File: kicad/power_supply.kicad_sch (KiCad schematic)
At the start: 16 parts, among them T1 reuse / AnTek AS-0524, U1 LM317T

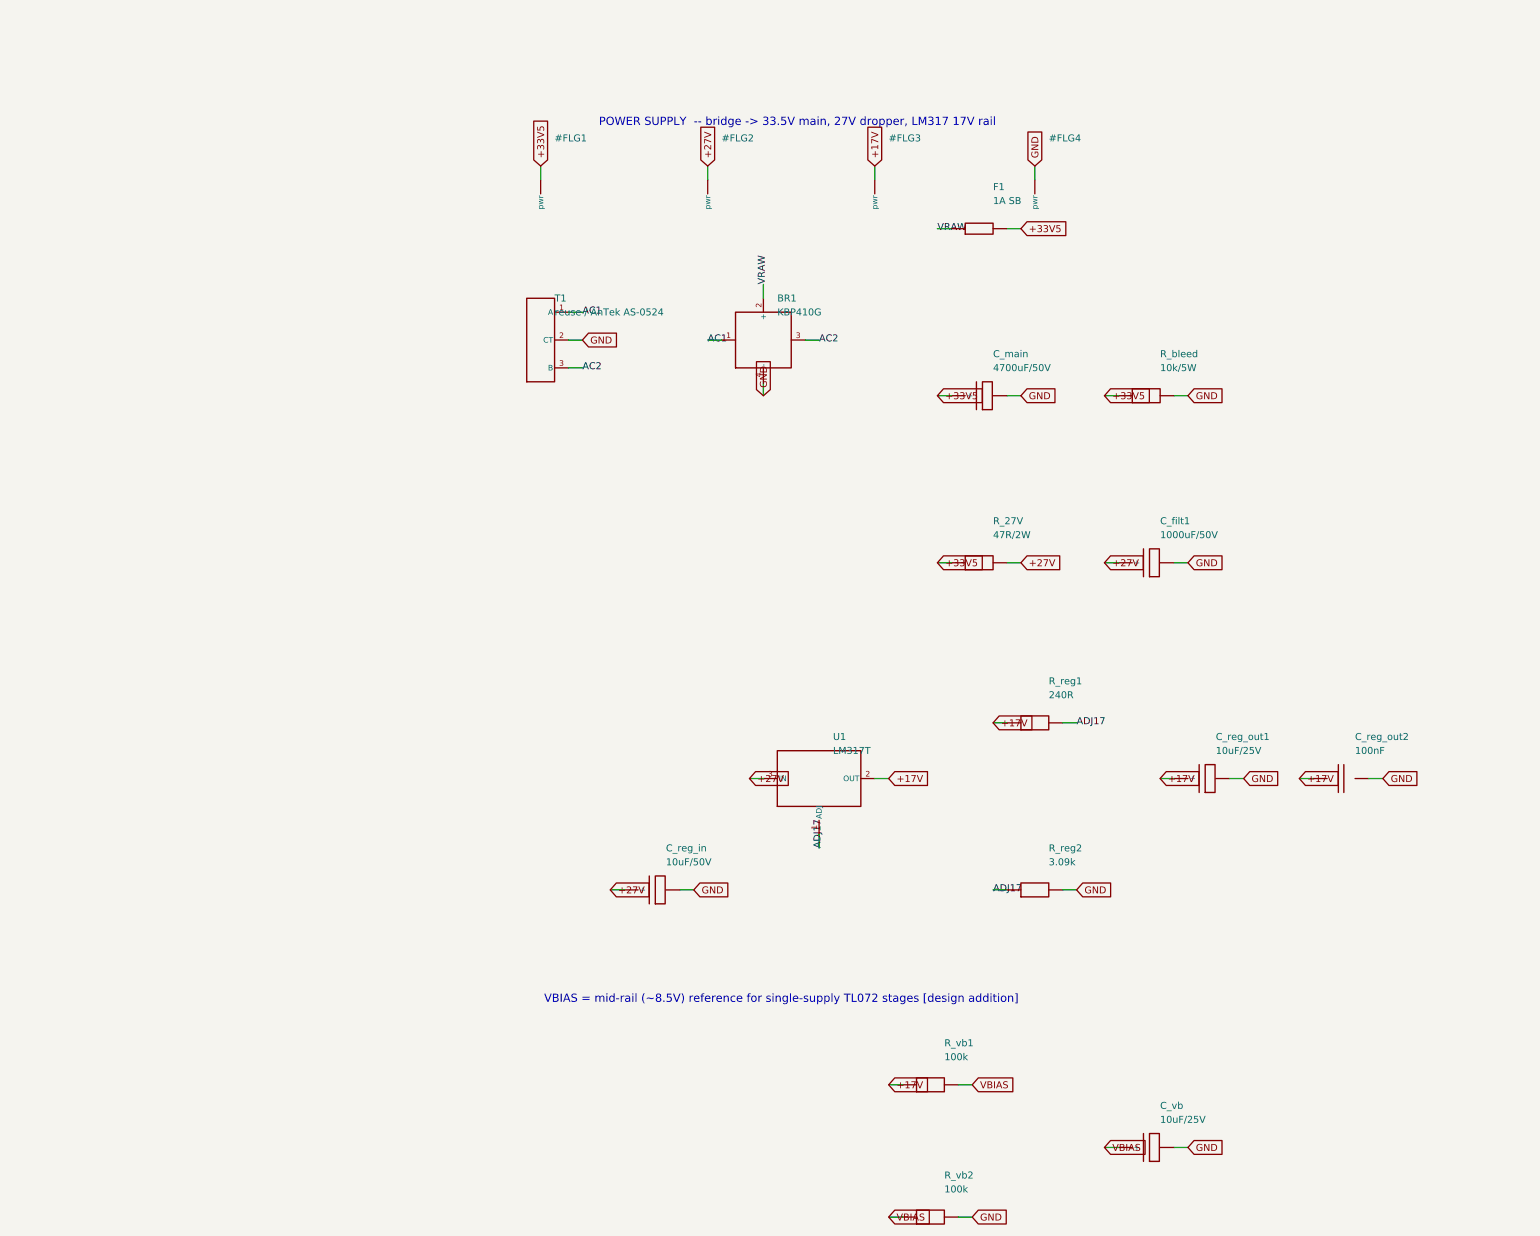
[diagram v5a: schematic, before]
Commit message: Keep LM317-input pre-filter (rename +27V->VREG_IN, 47R->100R) - corrected call
On reflection my earlier "delete R_27V, feed LM317 from +33.5V" recommendation
was wrong for a noise-conscious design: R_27V + C_filt1 is an RC pre-filter on
the LM317 input AND decouples the preamp supply from the power amp's transient
current draw on the +33.5V rail (the LM317's PSRR alone falls off with
frequency). Deleting it would hurt noise.

The real bug was the mislabeling: under the modern ~15 mA load the node sits at
~32 V, not 27 V, so the "27 V rail / 26-28 V" naming was a leftover misnomer.

Done instead:
- keep the element; bump 47R/2W -> 100R/1W (~6 dB more 120 Hz ripple rejection,
  ~1.5 V drop at 15 mA, LM317 in-out diff 14.7 V << 40 V max, ~0.02 W)
- rename net +27V -> VREG_IN (schematic gen, .kicad_pro Power pattern)
- correct the docs/troubleshooting voltages (~31-33 V) across Part 1/2/3/4,
  errata, BOM, availability-audit, PCB-NOTES/AUDIT, SCHEMATIC-BUILD, CHECKLIST

Verified: sch erc 0, full DRC unchanged (164), demo DRC 0, SPICE exit 0, BOM
CSV clean, net classes intact (VREG_IN now in the Power pattern).

https://claude.ai/code/session_01PkrfUi9tvZfLvudJ7h23qD
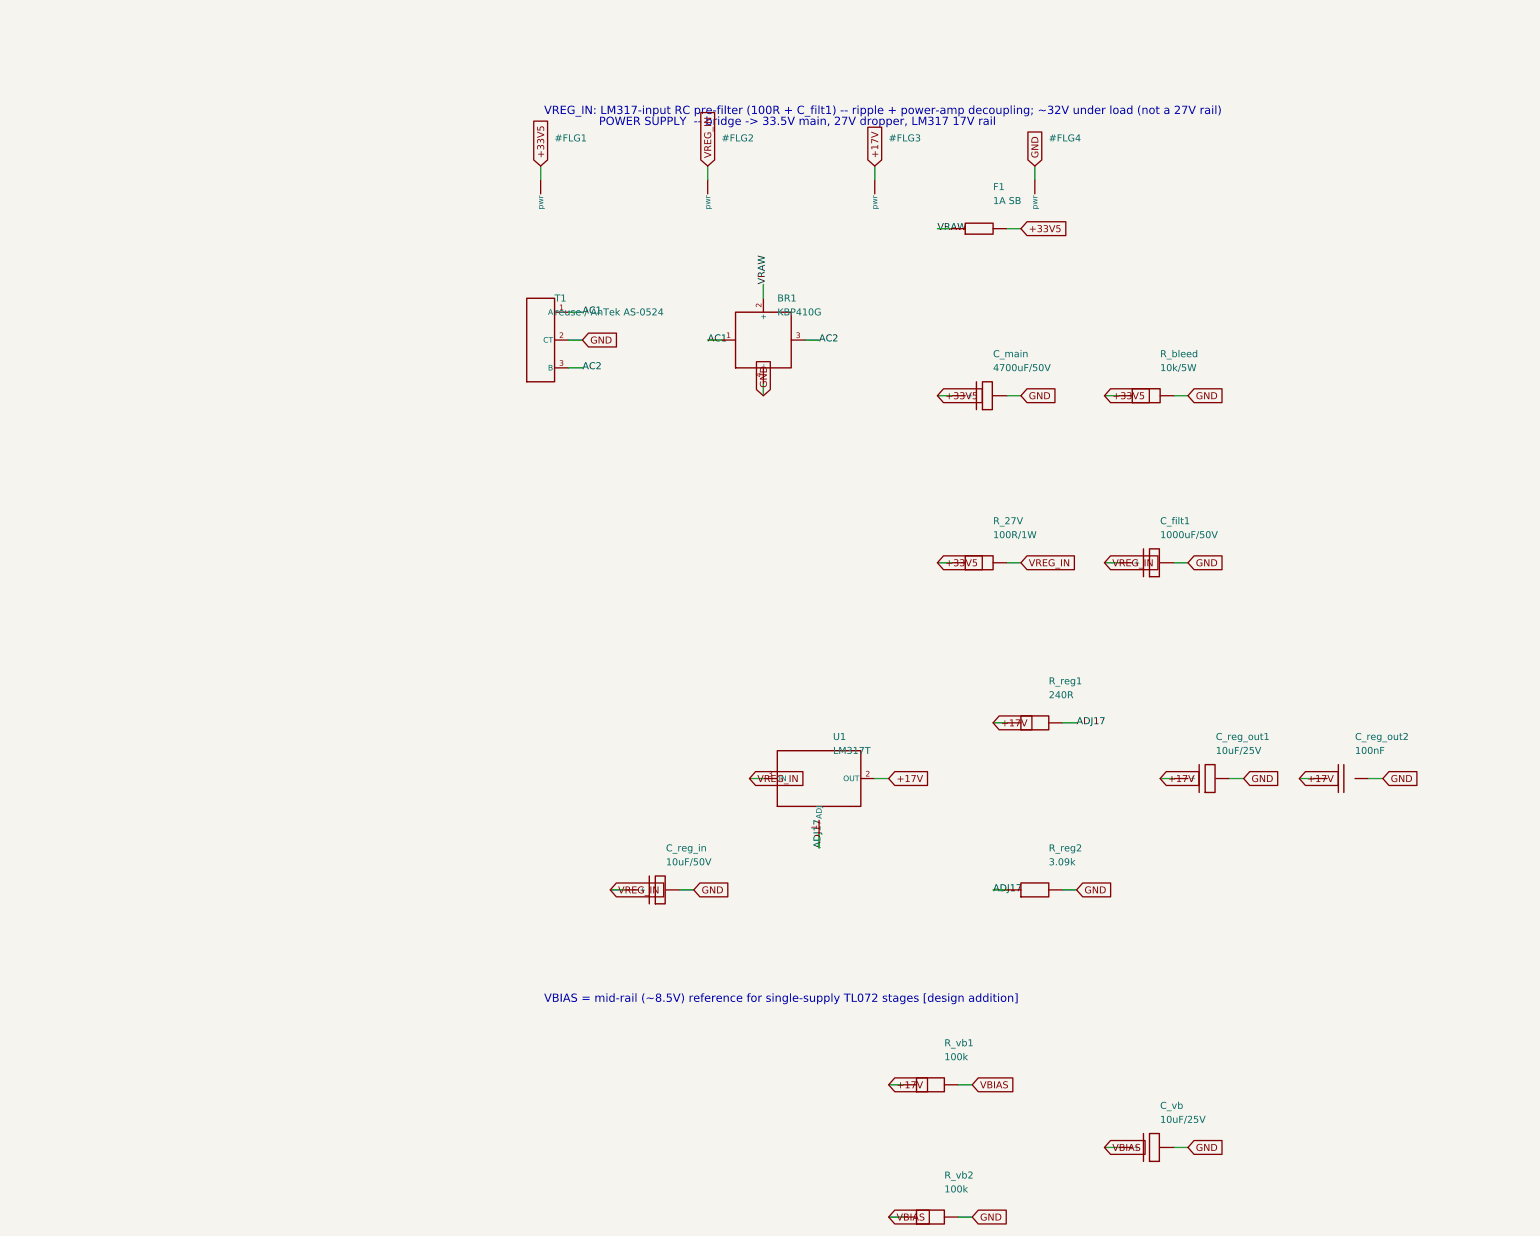
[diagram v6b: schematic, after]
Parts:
- R_27V: value 47R/2W -> 100R/1W
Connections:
- net +27V renamed VREG_IN
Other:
- note added: "VREG_IN: LM317-input RC pre-filter (100R + C_filt1) -- ripple + power-amp decoupling; ~32V under load (not a 27V rail)"

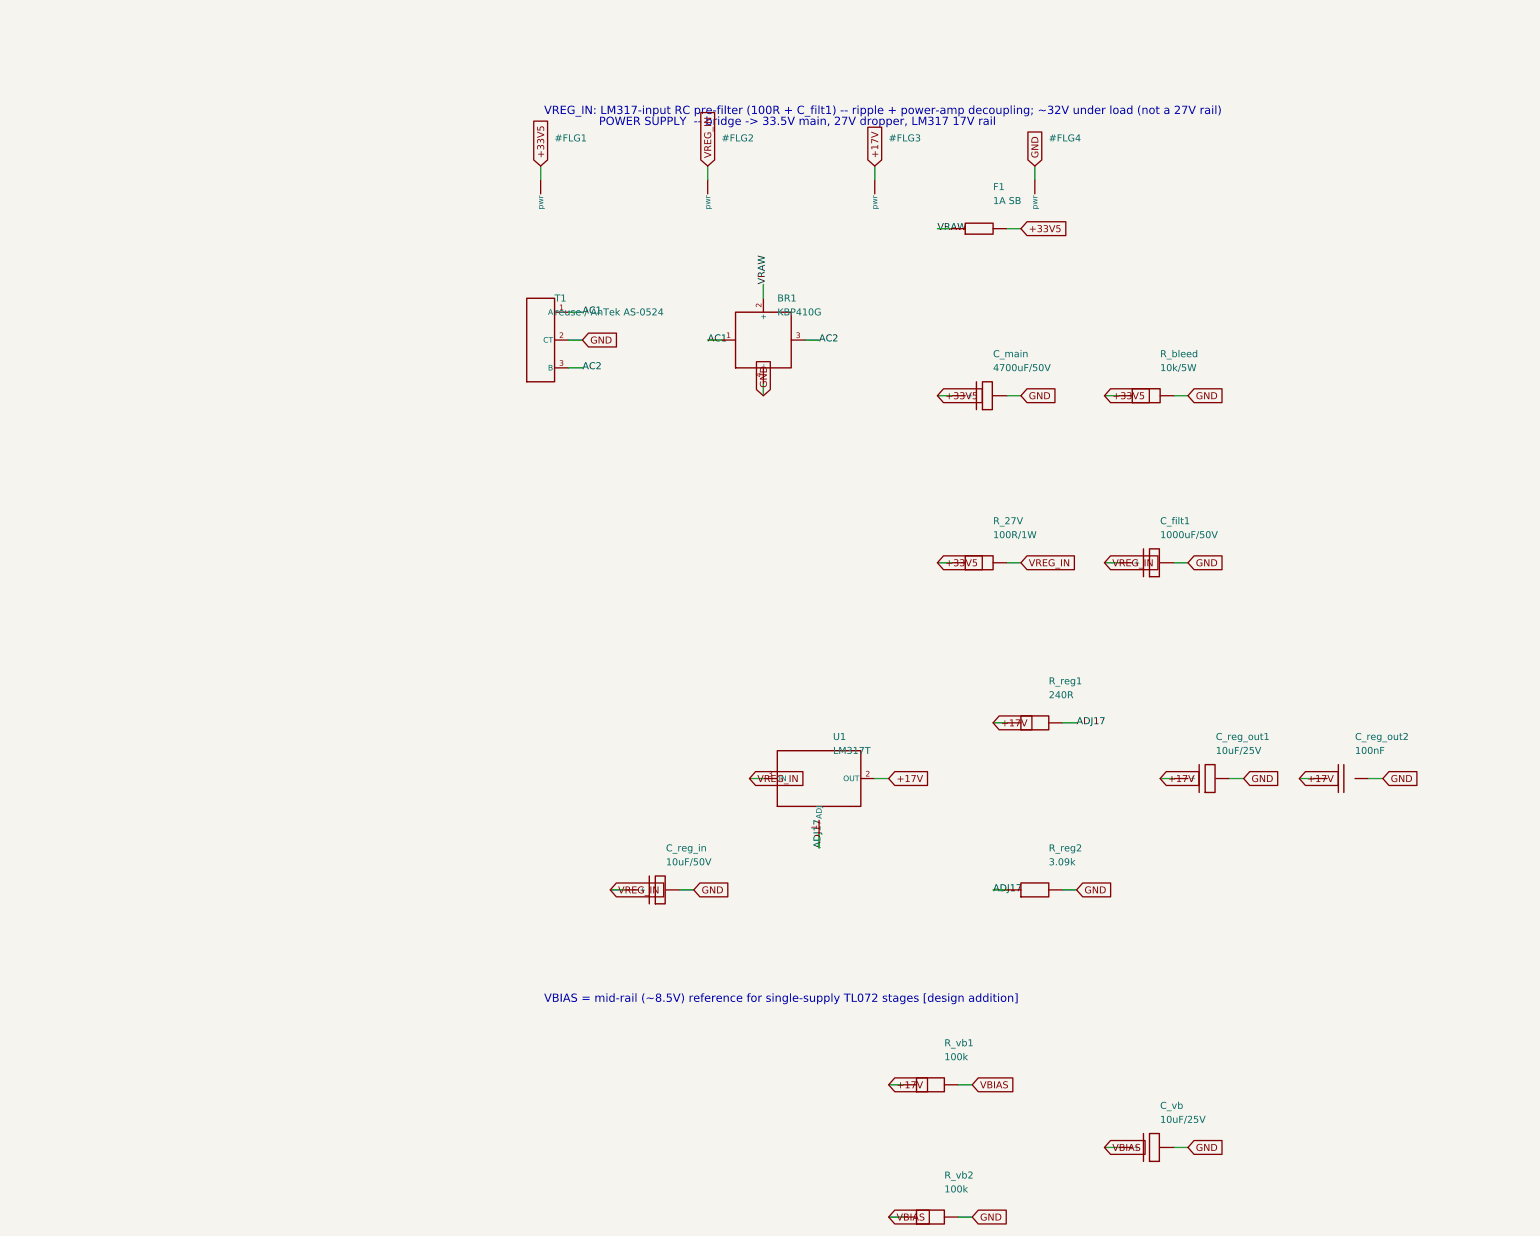
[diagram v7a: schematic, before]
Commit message: Redesign effects chain: active reverb summer + output buffer + split bias
Resolves roast R3 (broken passive mixer) and R6 (shared VBIAS bleed), using the
two spare TL072 halves and verifying with a rail-aware SPICE model.

- Reverb wet/dry mix is now an ACTIVE inverting summer on IC1-B (dry always on,
  wet via POT_REV, unity each, low-Z out about VBIAS_R). Removed the broken
  passive R_dry_tap/R_blend1/R_blend2 (1M dry series made it ~all-wet into an
  unbuffered 110k node).
- IC2-B repurposed as the post-MRB OUTPUT BUFFER driving PA_IN (removed the
  unbuffered R_painput 1M and a dead C_trem_out/R_trem_pass branch).
- VBIAS split into independent VBIAS_R (reverb) and VBIAS_T (tremolo) dividers
  (100k/100k + 47uF each) -> the LFO can no longer modulate the reverb reference.

Verification: new models/opamp_rail.sub clamps the output to the rails (unlike
opamp1p.sub), and spice/tran_reverb_mixer.cir confirms on a single +17V supply:
mid-rail bias 8.50 V, unity (0.0 dB) sum, clips at 15.5/1.5 V -> +-7 V headroom
(~24 dB over a 0.42 V program peak). This is the large-signal/headroom check the
rail-less model could not do (roast R7).

ERC 0; demo DRC 0; full board regenerated (106 footprints); run_all.sh exit 0;
BOM + roast doc + SCHEMATIC-BUILD + spice/README + CHANGELOG updated.

https://claude.ai/code/session_01PkrfUi9tvZfLvudJ7h23qD
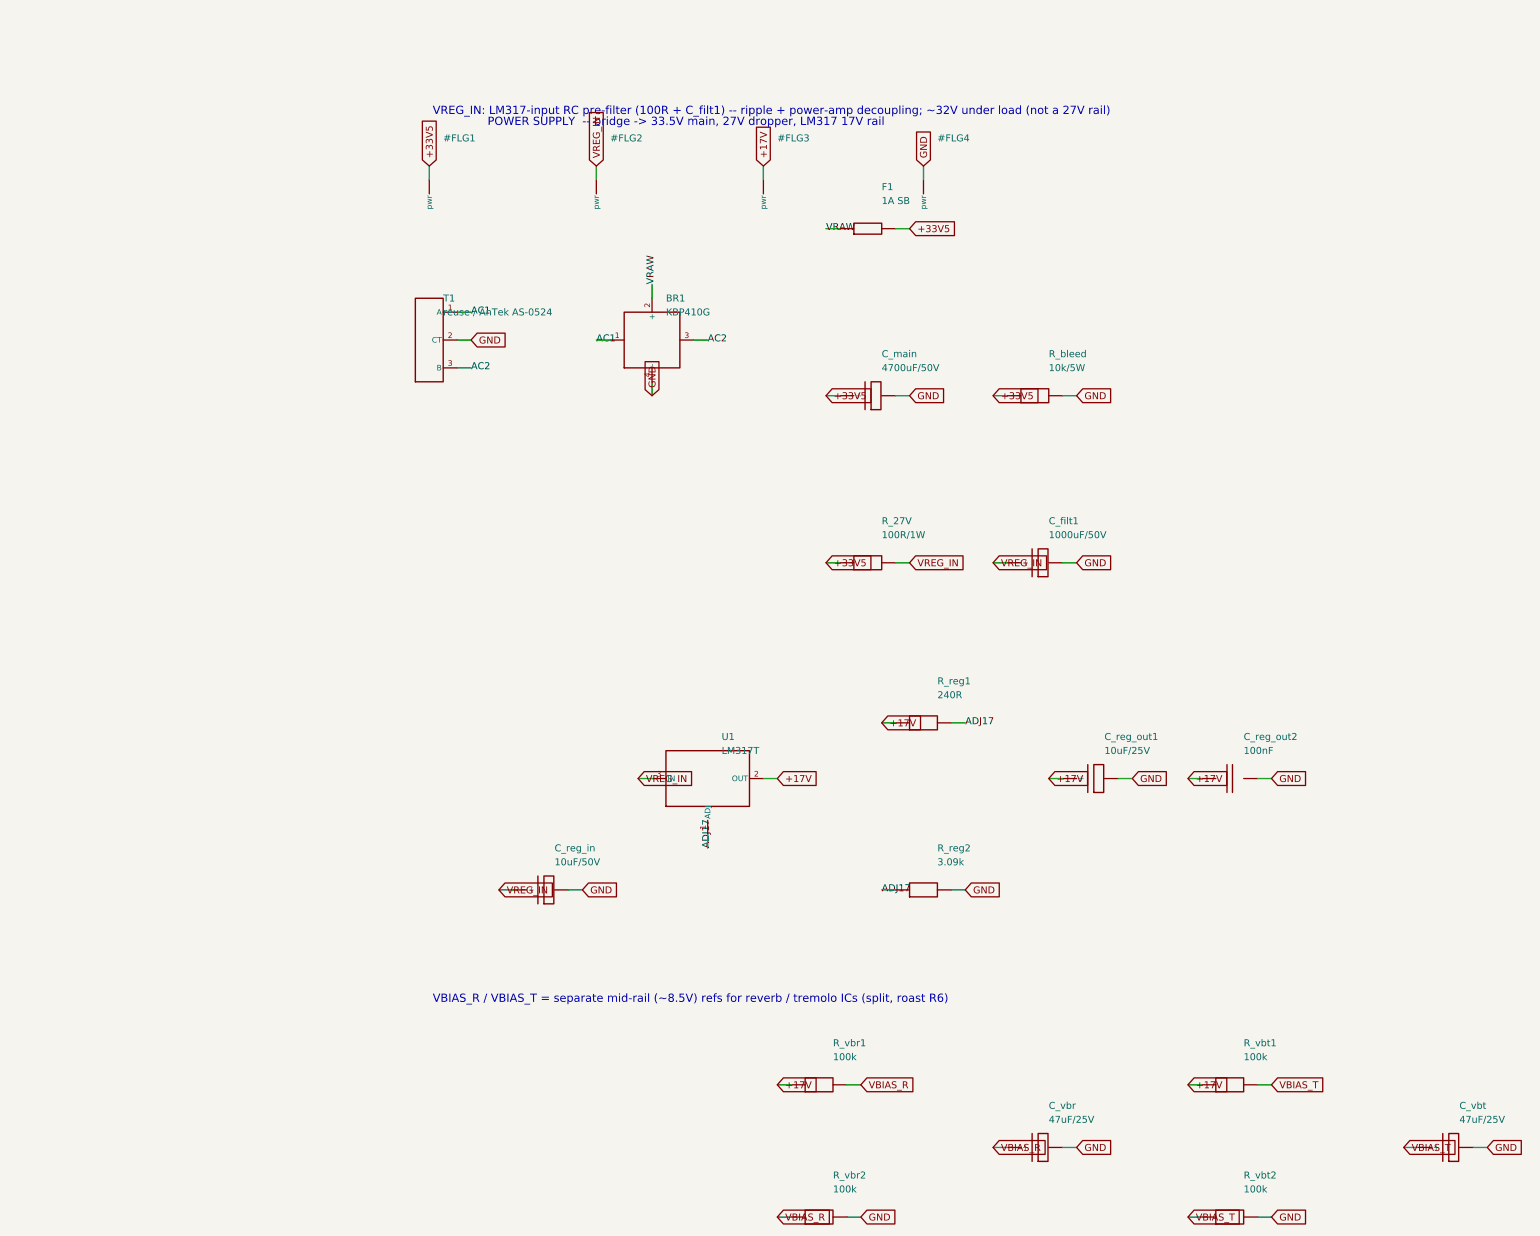
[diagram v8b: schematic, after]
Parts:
- removed C_vb: 10uF/25V, Capacitor_THT:CP_Radial_D8.0mm_P3.50mm, symbol cr_primitives:CP
- removed R_vb1, R_vb2: 100k, Resistor_THT:R_Axial_DIN0207_L6.3mm_D2.5mm_P5.08mm_Vertical, symbol cr_primitives:R
- added C_vbr, C_vbt: 47uF/25V, Capacitor_THT:CP_Radial_D8.0mm_P3.50mm, symbol cr_primitives:CP
- added R_vbr1, R_vbr2, R_vbt1, R_vbt2: 100k, Resistor_THT:R_Axial_DIN0207_L6.3mm_D2.5mm_P5.08mm_Vertical, symbol cr_primitives:R
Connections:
- net +17V: now also R_vbr1.1, R_vbt1.1
- net GND: now also C_vbr.2, C_vbt.2, R_vbr2.2, R_vbt2.2
- new net VBIAS_R: C_vbr.1 (+), R_vbr1.2, R_vbr2.1
- new net VBIAS_T: C_vbt.1 (+), R_vbt1.2, R_vbt2.1
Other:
- note added: "VBIAS_R / VBIAS_T = separate mid-rail (~8.5V) refs for reverb / tremolo ICs (split, roast R6)"
- note removed: "VBIAS = mid-rail (~8.5V) reference for single-supply TL072 stages [design addition]"
